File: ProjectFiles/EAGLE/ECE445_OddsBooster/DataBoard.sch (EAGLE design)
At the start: 12 parts, among them U2 74LV164D-SHIFT_REGISTER, U3 74LV164D-SHIFT_REGISTER, U4 74LV164D-SHIFT_REGISTER, X1 FH12-40S-0.5SH

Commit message: better design doc
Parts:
- added C10: 150u, rcl:C-USC0805
- added C2: 68u, rcl:C-USC0805
- added C3: 33u, rcl:C-USC0805
- added C4: 100p, rcl:C-USC0805
- added C5: 0.1p, rcl:C-USC0805
- added C6: 150p, rcl:C-USC0805
- added C7: 4.7u, rcl:C-USC0805
- added C8: 100u, rcl:C-USC0805
- added C9, CSP, C_IN: 0.1u, rcl:C-USC0805
- added CFB: 180p, rcl:C-USC0805
- added CZ: 0.01u, rcl:C-USC0805
- added C_OUT: 10u, rcl:C-USC0805
- added D1: Diode, diode:1N821
- added D2: DIODE, ngspice-simulation:DIODE
- added L: 10u, rcl:L-USL1812
- added L1: 3.3u, rcl:L-USL2825P
- added LP3965-ADJ: (no value), pinhead:PINHD-1X5
- added MIC2169: (no value), pinhead:PINHD-2X5
- added R10: 2, rcl:R-US_R0805
- added R11: 560, rcl:R-US_R0805
- added R12, RFB2: 8.2k, rcl:R-US_R0805
- added R13: 1.5k, rcl:R-US_R0805
- added R14: 1k, pot:TRIM_US-3223G
- added R15: 2k, pot:TRIM_US-SM-42/43B
- added R4, R7: 10k, rcl:R-US_R0805
- added R5, R6: 33k, rcl:R-US_R0805
- added R8: 2k, pot:TRIM_US-3223G
- added R9: 4k, rcl:R-US_R0805
- added RDUTY: 240k, rcl:R-US_R0805
- added RFB1: 82k, rcl:R-US_R0805
- added ROSC: 280k, rcl:R-US_R0805
- added RZ: 200k, rcl:R-US_R0805
- added S-8337ABIA-T8T1U: (no value), pinhead:PINHD-2X4
- added X2: (no value), con-berg:PN61729
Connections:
- new net N$1: C7.1, D1.A, MIC2169.3
- new net N$10: MIC2169.5, R11.1
- new net N$11: C9.1, D1.C, MIC2169.2
- new net N$12: C5.1, C6.1, MIC2169.7
- new net N$13: MIC2169.9, R12.1, R13.2
- new net N$14: R13.1, R14.E
- new net N$15: D2.A, L.2
- new net N$16: CSP.1, S-8337ABIA-T8T1U.5
- new net N$17: S-8337ABIA-T8T1U.8
- new net N$19: CZ.1, RZ.1
- new net N$2: R5.2, R6.2, R8.A
- new net N$20: RZ.2, S-8337ABIA-T8T1U.1
- new net N$21: CFB.2, RFB1.1, RFB2.2, S-8337ABIA-T8T1U.3
- new net N$22: ROSC.2, S-8337ABIA-T8T1U.4
- new net N$23: RDUTY.2, S-8337ABIA-T8T1U.2
- new net N$24: R15.E, RFB2.1
- new net N$3: C4.2, LP3965-ADJ.5, R4.2, R5.1, R6.1
- new net N$4: C9.2, L1.1, R10.2
- new net N$5: MIC2169.8
- new net N$6: MIC2169.6, R10.1
- new net N$7: MIC2169.4
- new net N$8: LP3965-ADJ.1, R7.2
- new net N$9: C5.2, R9.2
- new net V_BAT: C2.1, C_IN.1, L.1, LP3965-ADJ.2, S-8337ABIA-T8T1U.7
- new net V_CHARGE: C10.1, L1.2, R12.2
- new net V_USB: C8.1, MIC2169.1, R11.2, X2.1
- net GND: now also C10.2, C2.2, C3.2, C6.2, C7.2, C8.2, CSP.2, CZ.2, C_IN.2, C_OUT.2, LP3965-ADJ.3, MIC2169.10, R14.A, R15.S, R4.1, R7.1, R9.1, RDUTY.1, ROSC.1, S-8337ABIA-T8T1U.6, X2.4
- net VCC: now also C3.1, C4.1, LP3965-ADJ.4, R8.S
- net VDD: now also CFB.1, C_OUT.1, D2.C, RFB1.2

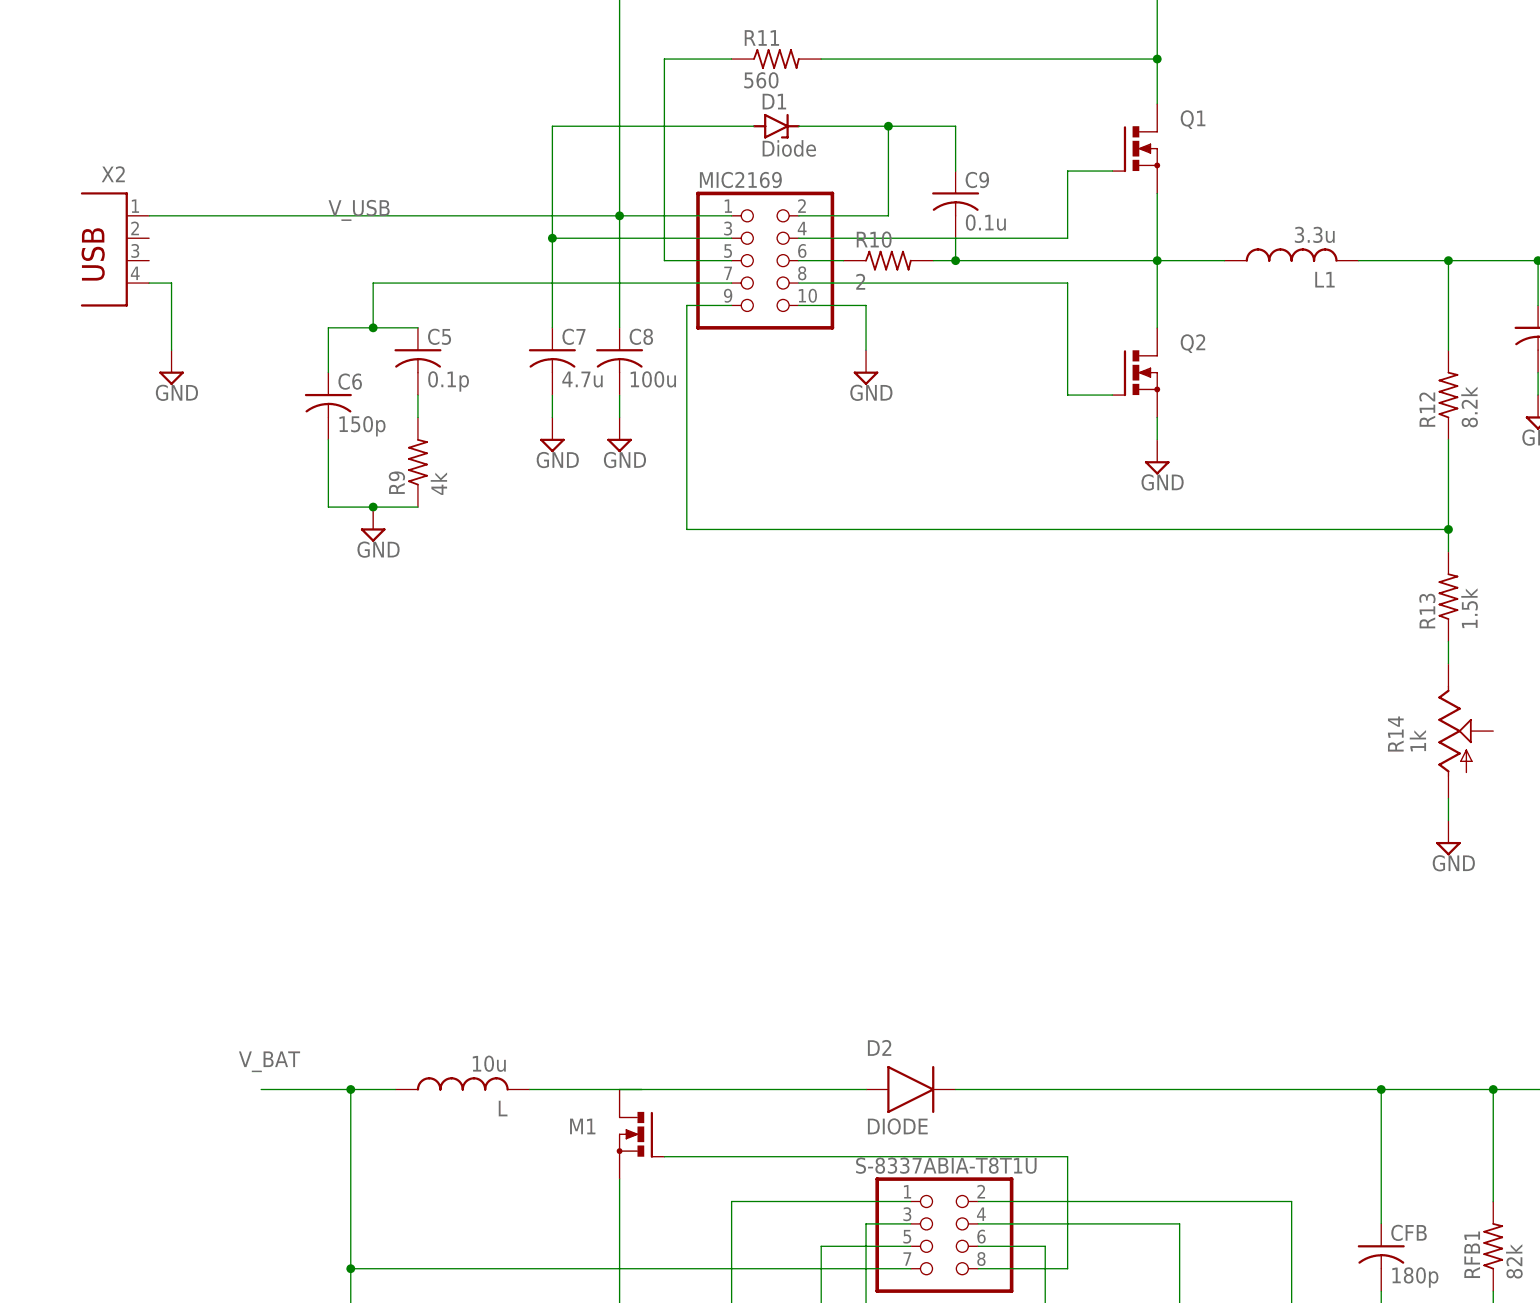
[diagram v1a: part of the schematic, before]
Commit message: Comms and display layout
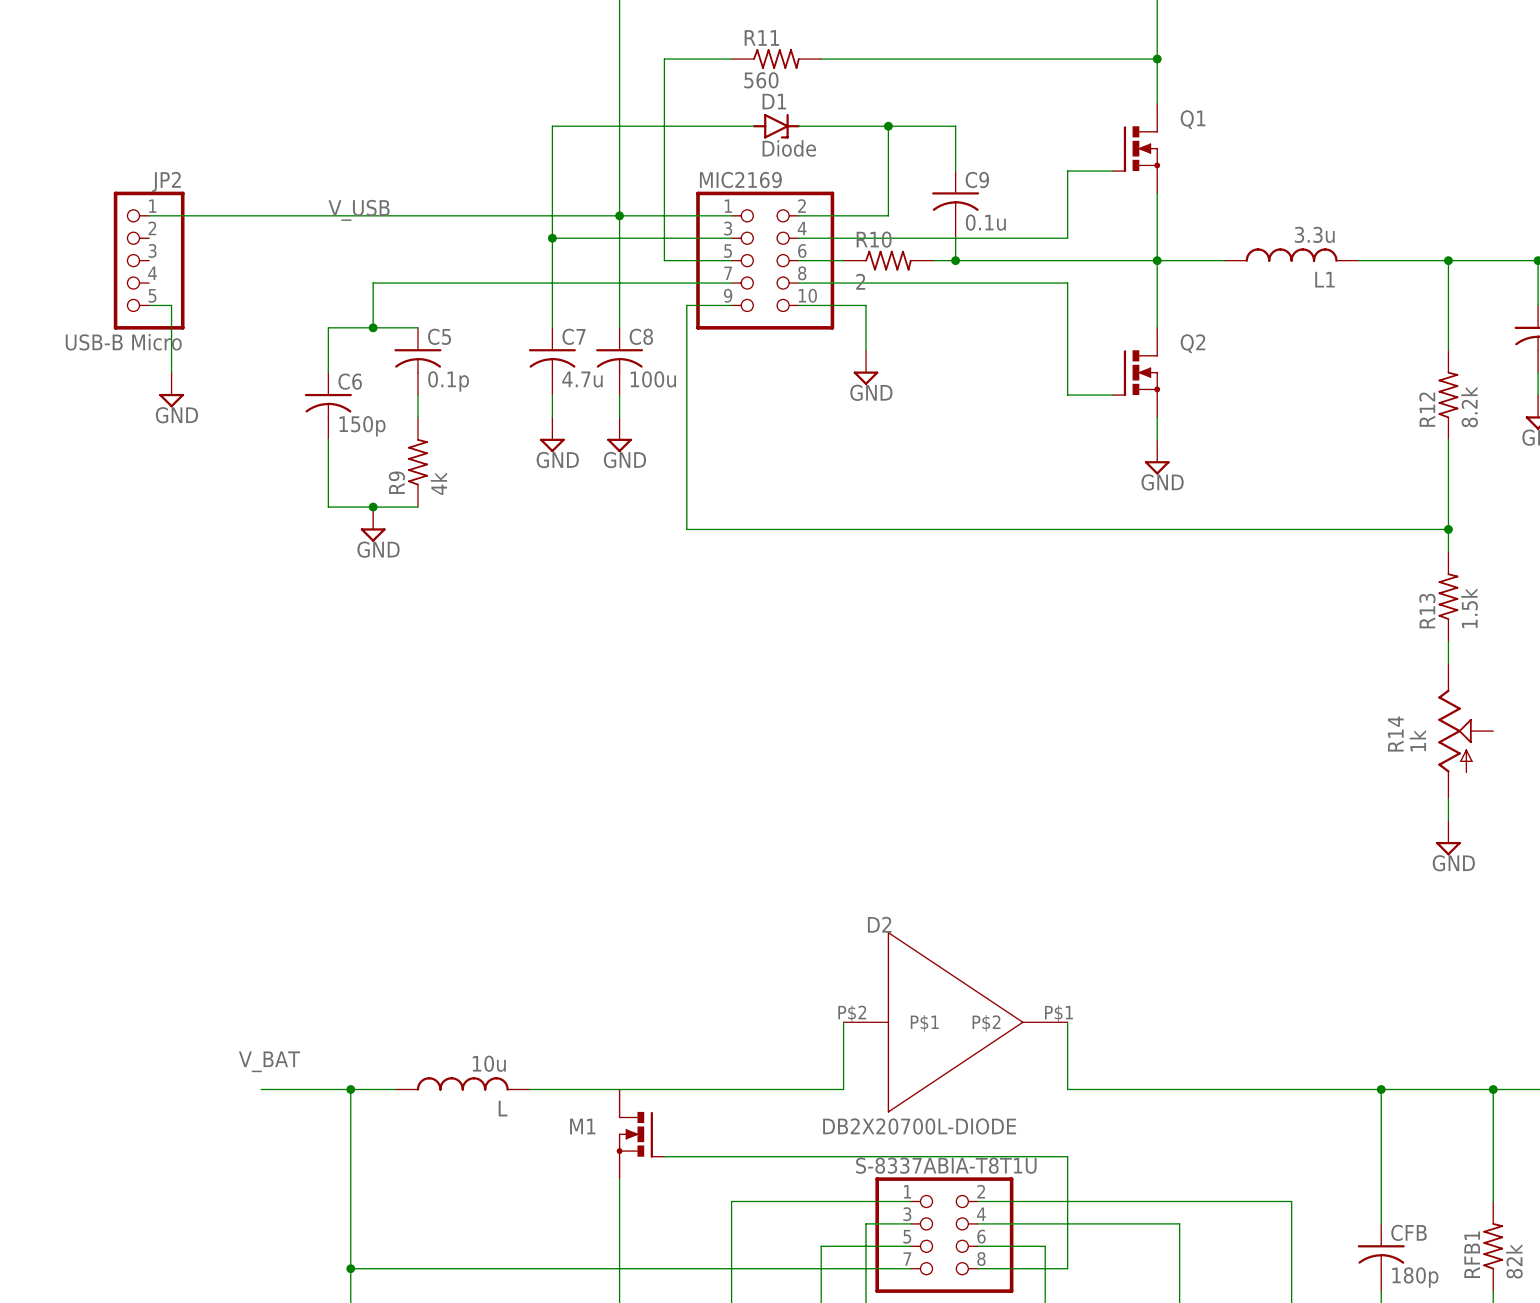
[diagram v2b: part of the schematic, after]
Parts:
- removed X2: (no value), con-berg:PN61729
- added JP2: USB-B Micro, pinhead:PINHD-1X5
- D2: value DIODE -> DB2X20700L-DIODE; device ngspice-simulation:DIODE -> OddsBooster:DB2X20700L-DIODE
- U1: device ESP32_WROVER_E_Bluetooth_Module:ESP32-WROVER-E -> OddsBooster:ESP32-WROVER-E
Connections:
- net GND: now also JP2.5; no longer X2.4
- net N$15: now also D2.P$1; no longer D2.A
- net VDD: now also D2.P$2; no longer D2.C
- net V_USB: now also JP2.1; no longer X2.1
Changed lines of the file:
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@@
 </classes>
 <parts>
-<part name="U1" library="ESP32_WROVER_E_Bluetooth_Module" deviceset="ESP32-WROVER-E" device=""/>
+<part name="U1" library="OddsBooster" deviceset="ESP32-WROVER-E" device=""/>
 <part name="SUPPLY3" library="supply2" library_urn="urn:adsk.eagle:library:372" deviceset="GND" device=""/>
 <part name="C1" library="rcl" library_urn="urn:adsk.eagle:library:334" deviceset="C-US" device="C0805" package3d_urn="urn:adsk.eagle:package:23617/2" value="0.1u"/>
@@
 <part name="R13" library="rcl" library_urn="urn:adsk.eagle:library:334" deviceset="R-US_" device="R0805" package3d_urn="urn:adsk.eagle:package:23553/2" value="1.5k"/>
 <part name="R14" library="pot" library_urn="urn:adsk.eagle:library:331" deviceset="TRIM_US-" device="3223G" package3d_urn="urn:adsk.eagle:package:22722/1" value="1k"/>
-<part name="X2" library="con-berg" library_urn="urn:adsk.eagle:library:130" deviceset="PN61729" device="" package3d_urn="urn:adsk.eagle:package:6148/1"/>
 <part name="SUPPLY24" library="supply2" library_urn="urn:adsk.eagle:library:372" deviceset="GND" device=""/>
 <part name="RZ" library="rcl" library_urn="urn:adsk.eagle:library:334" deviceset="R-US_" device="R0805" package3d_urn="urn:adsk.eagle:package:23553/2" value="200k"/>
@@
 <part name="C_OUT" library="rcl" library_urn="urn:adsk.eagle:library:334" deviceset="C-US" device="C0805" package3d_urn="urn:adsk.eagle:package:23617/2" value="10u"/>
 <part name="S-8337ABIA-T8T1U" library="pinhead" library_urn="urn:adsk.eagle:library:325" deviceset="PINHD-2X4" device="" package3d_urn="urn:adsk.eagle:package:22461/2"/>
-<part name="D2" library="ngspice-simulation" library_urn="urn:adsk.eagle:library:527439" deviceset="DIODE" device=""/>
 <part name="M1" library="transistor-power" library_urn="urn:adsk.eagle:library:400" deviceset="N-MOSFET_SYMBOL" device=""/>
 <part name="L" library="rcl" library_urn="urn:adsk.eagle:library:334" deviceset="L-US" device="L1812" package3d_urn="urn:adsk.eagle:package:23494/2" value="10u"/>
@@
 <part name="SUPPLY25" library="supply2" library_urn="urn:adsk.eagle:library:372" deviceset="GND" device=""/>
 <part name="R15" library="pot" library_urn="urn:adsk.eagle:library:331" deviceset="TRIM_US-" device="SM-42/43B" package3d_urn="urn:adsk.eagle:package:22717/1" value="2k"/>
+<part name="JP2" library="pinhead" library_urn="urn:adsk.eagle:library:325" deviceset="PINHD-1X5" device="" package3d_urn="urn:adsk.eagle:package:22469/2" value="USB-B Micro"/>
+<part name="D2" library="OddsBooster" deviceset="DB2X20700L-DIODE" device=""/>
 </parts>
 <sheets>
@@
 <attribute name="VALUE" x="-68.58" y="-104.14" size="1.778" layer="96" rot="R90"/>
 </instance>
-<instance part="X2" gate="G$1" x="-215.9" y="-48.26" smashed="yes" rot="MR0">
-<attribute name="NAME" x="-215.9" y="-39.37" size="1.778" layer="95" rot="MR0"/>
-<attribute name="VALUE" x="-215.9" y="-55.88" size="1.778" layer="96" rot="MR0"/>
-</instance>
-<instance part="SUPPLY24" gate="GND" x="-210.82" y="-60.96" smashed="yes">
-<attribute name="VALUE" x="-212.725" y="-64.135" size="1.778" layer="96"/>
+<instance part="SUPPLY24" gate="GND" x="-210.82" y="-63.5" smashed="yes">
+<attribute name="VALUE" x="-212.725" y="-66.675" size="1.778" layer="96"/>
 </instance>
 <instance part="RZ" gate="G$1" x="-147.32" y="-172.72" smashed="yes" rot="R90">
@@
 <attribute name="VALUE" x="-130.81" y="-167.64" size="1.778" layer="96"/>
 </instance>
-<instance part="D2" gate="G$1" x="-127" y="-142.24" smashed="yes">
-<attribute name="NAME" x="-132.08" y="-138.43" size="1.778" layer="95"/>
-<attribute name="VALUE" x="-132.08" y="-147.32" size="1.778" layer="96"/>
-</instance>
 <instance part="M1" gate="G$1" x="-157.48" y="-147.32" smashed="yes" rot="MR0">
 <attribute name="NAME" x="-162.56" y="-147.32" size="1.778" layer="95" rot="MR0"/>
@@
 <attribute name="NAME" x="-66.04" y="-195.58" size="1.778" layer="95" rot="R90"/>
 <attribute name="VALUE" x="-63.5" y="-195.58" size="1.778" layer="96" rot="R90"/>
+</instance>
+<instance part="JP2" gate="A" x="-215.9" y="-48.26" smashed="yes" rot="MR0">
+<attribute name="NAME" x="-209.55" y="-40.005" size="1.778" layer="95" rot="MR0"/>
+<attribute name="VALUE" x="-209.55" y="-58.42" size="1.778" layer="96" rot="MR0"/>
+</instance>
+<instance part="D2" gate="G$1" x="-111.76" y="-147.32" smashed="yes">
+<attribute name="NAME" x="-132.08" y="-124.46" size="1.778" layer="95"/>
+<attribute name="VALUE" x="-137.16" y="-147.32" size="1.778" layer="96"/>
 </instance>
 </instances>
@@
 </segment>
 <segment>
-<pinref part="X2" gate="G$1" pin="4"/>
-<wire x1="-213.36" y1="-50.8" x2="-210.82" y2="-50.8" width="0.1524" layer="91"/>
-<wire x1="-210.82" y1="-50.8" x2="-210.82" y2="-58.42" width="0.1524" layer="91"/>
+<wire x1="-213.36" y1="-53.34" x2="-210.82" y2="-53.34" width="0.1524" layer="91"/>
+<wire x1="-210.82" y1="-53.34" x2="-210.82" y2="-60.96" width="0.1524" layer="91"/>
 <pinref part="SUPPLY24" gate="GND" pin="GND"/>
+<pinref part="JP2" gate="A" pin="5"/>
 </segment>
 <segment>
@@
 </segment>
 <segment>
-<pinref part="D2" gate="G$1" pin="C"/>
-<wire x1="-121.92" y1="-142.24" x2="-73.66" y2="-142.24" width="0.1524" layer="91"/>
 <pinref part="CFB" gate="G$1" pin="1"/>
 <wire x1="-73.66" y1="-142.24" x2="-60.96" y2="-142.24" width="0.1524" layer="91"/>
 <wire x1="-60.96" y1="-142.24" x2="-43.18" y2="-142.24" width="0.1524" layer="91"/>
 <wire x1="-73.66" y1="-157.48" x2="-73.66" y2="-142.24" width="0.1524" layer="91"/>
-<junction x="-73.66" y="-142.24"/>
 <pinref part="RFB1" gate="G$1" pin="2"/>
 <wire x1="-60.96" y1="-154.94" x2="-60.96" y2="-142.24" width="0.1524" layer="91"/>
@@
 <junction x="-43.18" y="-142.24"/>
 <label x="-33.02" y="-139.7" size="1.778" layer="95"/>
+<pinref part="D2" gate="G$1" pin="P$2"/>
+<wire x1="-109.22" y1="-134.62" x2="-109.22" y2="-142.24" width="0.1524" layer="91"/>
+<wire x1="-109.22" y1="-142.24" x2="-73.66" y2="-142.24" width="0.1524" layer="91"/>
+<junction x="-73.66" y="-142.24"/>
 </segment>
 </net>
@@
 <junction x="-99.06" y="-25.4"/>
 <label x="-193.04" y="-43.18" size="1.778" layer="95"/>
-<pinref part="X2" gate="G$1" pin="1"/>
+<pinref part="JP2" gate="A" pin="1"/>
 </segment>
 </net>
@@
 </segment>
 </net>
-<net name="N$15" class="0">
-<segment>
-<pinref part="L" gate="G$1" pin="2"/>
-<pinref part="D2" gate="G$1" pin="A"/>
-<wire x1="-132.08" y1="-142.24" x2="-170.18" y2="-142.24" width="0.1524" layer="91"/>
-</segment>
-</net>
 <net name="N$16" class="0">
 <segment>
@@
 <wire x1="-109.22" y1="-162.56" x2="-109.22" y2="-149.86" width="0.1524" layer="91"/>
 <wire x1="-109.22" y1="-149.86" x2="-154.94" y2="-149.86" width="0.1524" layer="91"/>
-</segment>
-</net>
-<net name="N$18" class="0">
-<segment>
-<wire x1="-157.48" y1="-142.24" x2="-160.02" y2="-142.24" width="0.1524" layer="91"/>
 </segment>
 </net>
@@
 </segment>
 </net>
+<net name="N$15" class="0">
+<segment>
+<pinref part="L" gate="G$1" pin="2"/>
+<wire x1="-170.18" y1="-142.24" x2="-134.62" y2="-142.24" width="0.1524" layer="91"/>
+<pinref part="D2" gate="G$1" pin="P$1"/>
+<wire x1="-134.62" y1="-142.24" x2="-134.62" y2="-134.62" width="0.1524" layer="91"/>
+</segment>
+</net>

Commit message: layout minor changes
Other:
- moved on the sheet: U2, U3, U4, X1-1, X1-10, X1-11, X1-12, X1-13, X1-14, X1-15, X1-16, X1-17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

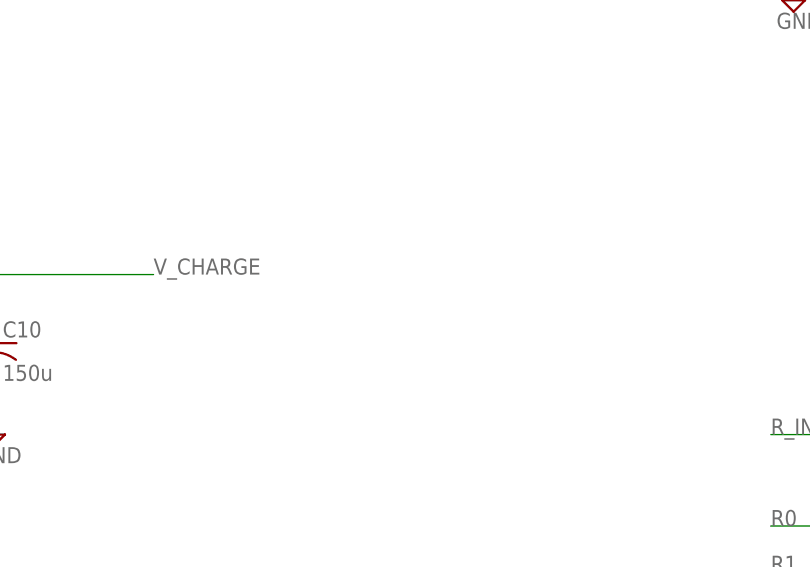
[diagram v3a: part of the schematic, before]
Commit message: updated data sheets and some layout changes
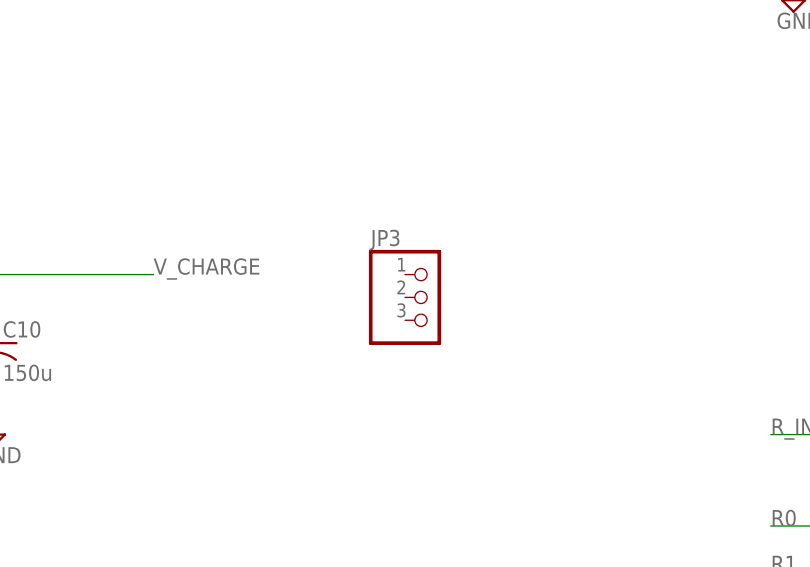
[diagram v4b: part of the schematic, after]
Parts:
- added JP3: (no value), pinhead:PINHD-1X3
- C8: device rcl:C-USC0805 -> rcl:C-USC1210
